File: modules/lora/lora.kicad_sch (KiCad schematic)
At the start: 6 parts, among them U1 RFM95W-868S2

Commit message: Updating all modules
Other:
- moved on the sheet: C1, C2, C3, C4, R1, U1

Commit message: Updating lora module
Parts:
- C1, C2, C3, C4: footprint (none) -> Capacitor_SMD:C_0603_1608Metric
- R1: footprint (none) -> Resistor_SMD:R_0603_1608Metric
- U1: footprint (none) -> RF_Module:HOPERF_RFM9XW_SMD
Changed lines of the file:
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@@
 			)
 		)
-		(property "Footprint" ""
+		(property "Footprint" "Capacitor_SMD:C_0603_1608Metric"
 			(at 120.65 62.23 0)
 			(effects
@@
 			)
 		)
-		(property "Footprint" ""
+		(property "Footprint" "Capacitor_SMD:C_0603_1608Metric"
 			(at 133.35 62.23 0)
 			(effects
@@
 			)
 		)
-		(property "Footprint" ""
+		(property "Footprint" "Resistor_SMD:R_0603_1608Metric"
 			(at 102.87 53.34 0)
 			(effects
@@
 			)
 		)
-		(property "Footprint" ""
+		(property "Footprint" "RF_Module:HOPERF_RFM9XW_SMD"
 			(at -1.27 19.05 0)
 			(effects
@@
 			)
 		)
-		(property "Footprint" ""
+		(property "Footprint" "Capacitor_SMD:C_0603_1608Metric"
 			(at 127 62.23 0)
 			(effects
@@
 			)
 		)
-		(property "Footprint" ""
+		(property "Footprint" "Capacitor_SMD:C_0603_1608Metric"
 			(at 107.95 57.15 0)
 			(effects

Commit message: Updating all schematics
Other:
- note added: "${project_name} ${project_version} ${project_creator} License: ${project_license} Year: ${project_year}"
- note added: "......"
- note added: "......."
- note added: "1"
- note added: "3D top side"
- note added: "CoverPage"
- note added: "Index"
- note added: "Page"
- company: (none) -> ${project_creator}
- title: (none) -> ${project_name}
- moved on the sheet: C1, C2, C3, C4, R1, U1

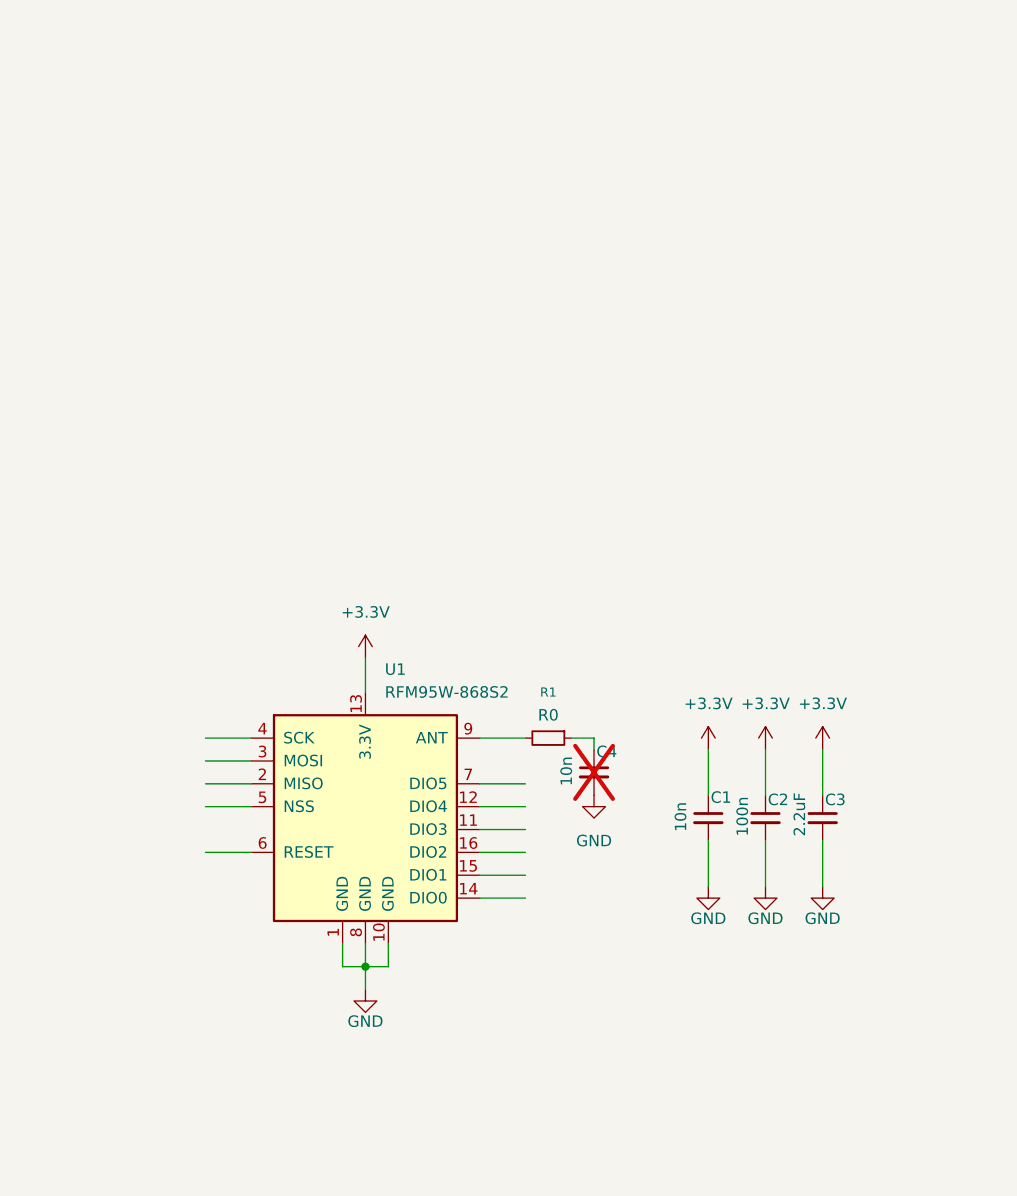
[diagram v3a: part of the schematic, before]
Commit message: Adding LoRa module
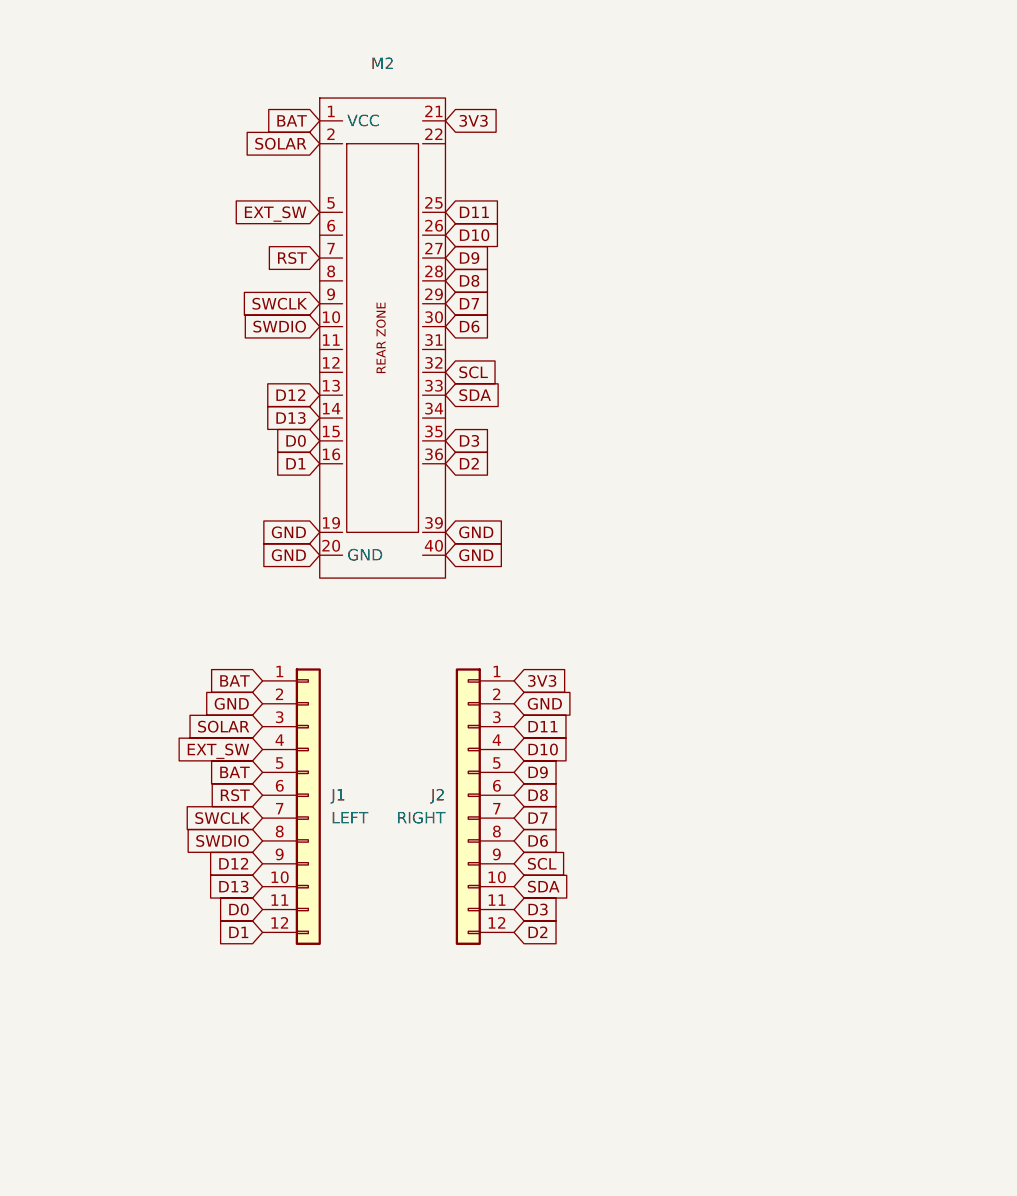
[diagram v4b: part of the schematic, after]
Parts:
- removed C1, C4: 10n, Capacitor_SMD:C_0603_1608Metric, symbol Device:C_Small
- removed C2: 100n, Capacitor_SMD:C_0603_1608Metric, symbol Device:C_Small
- removed C3: 2.2uF, Capacitor_SMD:C_0603_1608Metric, symbol Device:C_Small
- removed R1: R0, Resistor_SMD:R_0603_1608Metric, symbol Device:R_Small
- removed U1: RFM95W-868S2, RF_Module:HOPERF_RFM9XW_SMD, symbol RF_Module:RFM95W-868S2
- added J1: LEFT, Connector_PinSocket_2.54mm:PinSocket_1x12_P2.54mm_Vertical, symbol Connector_Generic:Conn_01x12
- added J2: RIGHT, Connector_PinSocket_2.54mm:PinSocket_1x12_P2.54mm_Vertical, symbol Connector_Generic:Conn_01x12
- added M2: ~, MegaCastle:MegaCastle2x20-Module-I40.0x46.0-MBCFFF3CFFF3-SPAREPAD, symbol MegaCastle:MegaCastle2x20-Module-I40.0x46.0-MBCFFF3CFFF3
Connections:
- net GND: now also J1.2 (Pin_2), J2.2 (Pin_2), M2.19, M2.20 (GND), M2.39, M2.40
- new net 3V3: J2.1 (Pin_1), M2.21
- new net BAT: J1.1 (Pin_1), J1.5 (Pin_5), M2.1 (VCC)
- new net D0: J1.11 (Pin_11), M2.15
- new net D1: J1.12 (Pin_12), M2.16
- new net D10: J2.4 (Pin_4), M2.26
- new net D11: J2.3 (Pin_3), M2.25
- new net D12: J1.9 (Pin_9), M2.13
- new net D13: J1.10 (Pin_10), M2.14
- new net D2: J2.12 (Pin_12), M2.36
- new net D3: J2.11 (Pin_11), M2.35
- new net D6: J2.8 (Pin_8), M2.30
- new net D7: J2.7 (Pin_7), M2.29
- new net D8: J2.6 (Pin_6), M2.28
- new net D9: J2.5 (Pin_5), M2.27
- new net EXT_SW: J1.4 (Pin_4), M2.5
- new net RST: J1.6 (Pin_6), M2.7
- new net SCL: J2.9 (Pin_9), M2.32
- new net SDA: J2.10 (Pin_10), M2.33
- new net SOLAR: J1.3 (Pin_3), M2.2
- new net SWCLK: J1.7 (Pin_7), M2.9
- new net SWDIO: J1.8 (Pin_8), M2.10
